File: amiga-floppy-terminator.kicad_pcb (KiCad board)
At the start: 2 copper layers, 7.7 x 59.5 mm, 2 parts, among them J1 Conn_02x17_Odd_Even

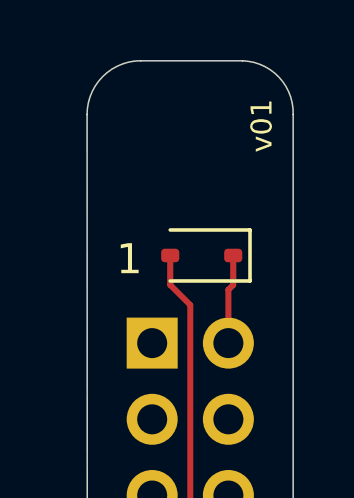
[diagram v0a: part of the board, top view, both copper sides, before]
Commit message: v02: Invert diode polarity
What I could do wrong, I did.

Both _DCD and _SEL0 are active low, hence the diode must be inverted to
point towards _SEL0.
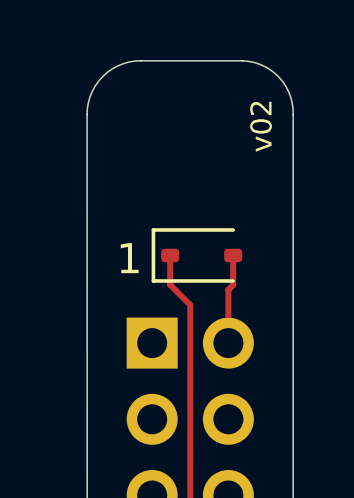
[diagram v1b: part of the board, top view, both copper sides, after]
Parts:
- turned D1 to 0 degrees
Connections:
- D1 pad 1: _DCD -> _SEL0
- D1 pad 2: _SEL0 -> _DCD
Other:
- board text added: "v02"
- board text removed: "v01"
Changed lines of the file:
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@@
 	(footprint "Diode_SMD:D_SOD-323"
 		(layer "F.Cu")
-		(at 101.6 59.563 180)
+		(at 101.6 59.563)
 		(descr "SOD-323")
 		(tags "SOD-323")
 		(property "Reference" "D1"
-			(at 0 -1.85 0)
+			(at 0 -1.85 360)
 			(layer "F.SilkS")
 			(hide yes)
@@
 		)
 		(property "Value" "D"
-			(at 0.1 1.9 0)
+			(at 0.1 1.9 360)
 			(layer "F.Fab")
 			(effects
@@
 		)
 		(property "Footprint" "Diode_SMD:D_SOD-323"
-			(at 0 0 180)
+			(at 0 0 0)
 			(unlocked yes)
 			(layer "F.Fab")
@@
 		)
 		(property "Datasheet" ""
-			(at 0 0 180)
+			(at 0 0 0)
 			(unlocked yes)
 			(layer "F.Fab")
@@
 		)
 		(property "Description" "Diode"
-			(at 0 0 180)
+			(at 0 0 0)
 			(unlocked yes)
 			(layer "F.Fab")
@@
 		)
 		(property "Sim.Device" "D"
-			(at 0 0 180)
+			(at 0 0 0)
 			(unlocked yes)
 			(layer "F.Fab")
@@
 		)
 		(property "Sim.Pins" "1=K 2=A"
-			(at 0 0 180)
+			(at 0 0 0)
 			(unlocked yes)
 			(layer "F.Fab")
@@
 		)
 		(property "LCSC" "C2128"
-			(at 0 0 180)
+			(at 0 0 0)
 			(unlocked yes)
 			(layer "F.Fab")
@@
 		(attr smd)
 		(fp_line
+			(start -1.61 -0.85)
+			(end -1.61 0.85)
+			(stroke
+				(width 0.12)
+				(type solid)
+			)
+			(layer "F.SilkS")
+		)
+		(fp_line
+			(start -1.61 -0.85)
+			(end 1.05 -0.85)
+			(stroke
+				(width 0.12)
+				(type solid)
+			)
+			(layer "F.SilkS")
+		)
+		(fp_line
 			(start -1.61 0.85)
 			(end 1.05 0.85)
@@
 		)
 		(fp_line
-			(start -1.61 -0.85)
-			(end 1.05 -0.85)
-			(stroke
-				(width 0.12)
-				(type solid)
-			)
-			(layer "F.SilkS")
-		)
-		(fp_line
-			(start -1.61 -0.85)
-			(end -1.61 0.85)
-			(stroke
-				(width 0.12)
-				(type solid)
-			)
-			(layer "F.SilkS")
+			(start -1.6 -0.95)
+			(end -1.6 0.95)
+			(stroke
+				(width 0.05)
+				(type solid)
+			)
+			(layer "F.CrtYd")
+		)
+		(fp_line
+			(start -1.6 -0.95)
+			(end 1.6 -0.95)
+			(stroke
+				(width 0.05)
+				(type solid)
+			)
+			(layer "F.CrtYd")
+		)
+		(fp_line
+			(start -1.6 0.95)
+			(end 1.6 0.95)
+			(stroke
+				(width 0.05)
+				(type solid)
+			)
+			(layer "F.CrtYd")
 		)
 		(fp_line
@@
 		)
 		(fp_line
-			(start -1.6 0.95)
-			(end 1.6 0.95)
-			(stroke
-				(width 0.05)
-				(type solid)
-			)
-			(layer "F.CrtYd")
-		)
-		(fp_line
-			(start -1.6 -0.95)
-			(end 1.6 -0.95)
-			(stroke
-				(width 0.05)
-				(type solid)
-			)
-			(layer "F.CrtYd")
-		)
-		(fp_line
-			(start -1.6 -0.95)
-			(end -1.6 0.95)
-			(stroke
-				(width 0.05)
-				(type solid)
-			)
-			(layer "F.CrtYd")
+			(start -0.9 -0.7)
+			(end 0.9 -0.7)
+			(stroke
+				(width 0.1)
+				(type solid)
+			)
+			(layer "F.Fab")
+		)
+		(fp_line
+			(start -0.9 0.7)
+			(end -0.9 -0.7)
+			(stroke
+				(width 0.1)
+				(type solid)
+			)
+			(layer "F.Fab")
+		)
+		(fp_line
+			(start -0.3 -0.35)
+			(end -0.3 0.35)
+			(stroke
+				(width 0.1)
+				(type solid)
+			)
+			(layer "F.Fab")
+		)
+		(fp_line
+			(start -0.3 0)
+			(end -0.5 0)
+			(stroke
+				(width 0.1)
+				(type solid)
+			)
+			(layer "F.Fab")
+		)
+		(fp_line
+			(start -0.3 0)
+			(end 0.2 -0.35)
+			(stroke
+				(width 0.1)
+				(type solid)
+			)
+			(layer "F.Fab")
+		)
+		(fp_line
+			(start 0.2 -0.35)
+			(end 0.2 0.35)
+			(stroke
+				(width 0.1)
+				(type solid)
+			)
+			(layer "F.Fab")
+		)
+		(fp_line
+			(start 0.2 0)
+			(end 0.45 0)
+			(stroke
+				(width 0.1)
+				(type solid)
+			)
+			(layer "F.Fab")
+		)
+		(fp_line
+			(start 0.2 0.35)
+			(end -0.3 0)
+			(stroke
+				(width 0.1)
+				(type solid)
+			)
+			(layer "F.Fab")
+		)
+		(fp_line
+			(start 0.9 -0.7)
+			(end 0.9 0.7)
+			(stroke
+				(width 0.1)
+				(type solid)
+			)
+			(layer "F.Fab")
 		)
 		(fp_line
@@
 			(layer "F.Fab")
 		)
-		(fp_line
-			(start 0.9 -0.7)
-			(end 0.9 0.7)
-			(stroke
-				(width 0.1)
-				(type solid)
-			)
-			(layer "F.Fab")
-		)
-		(fp_line
-			(start 0.2 0.35)
-			(end -0.3 0)
-			(stroke
-				(width 0.1)
-				(type solid)
-			)
-			(layer "F.Fab")
-		)
-		(fp_line
-			(start 0.2 0)
-			(end 0.45 0)
-			(stroke
-				(width 0.1)
-				(type solid)
-			)
-			(layer "F.Fab")
-		)
-		(fp_line
-			(start 0.2 -0.35)
-			(end 0.2 0.35)
-			(stroke
-				(width 0.1)
-				(type solid)
-			)
-			(layer "F.Fab")
-		)
-		(fp_line
-			(start -0.3 0)
-			(end 0.2 -0.35)
-			(stroke
-				(width 0.1)
-				(type solid)
-			)
-			(layer "F.Fab")
-		)
-		(fp_line
-			(start -0.3 0)
-			(end -0.5 0)
-			(stroke
-				(width 0.1)
-				(type solid)
-			)
-			(layer "F.Fab")
-		)
-		(fp_line
-			(start -0.3 -0.35)
-			(end -0.3 0.35)
-			(stroke
-				(width 0.1)
-				(type solid)
-			)
-			(layer "F.Fab")
-		)
-		(fp_line
-			(start -0.9 0.7)
-			(end -0.9 -0.7)
-			(stroke
-				(width 0.1)
-				(type solid)
-			)
-			(layer "F.Fab")
-		)
-		(fp_line
-			(start -0.9 -0.7)
-			(end 0.9 -0.7)
-			(stroke
-				(width 0.1)
-				(type solid)
-			)
-			(layer "F.Fab")
-		)
 		(fp_text user "${REFERENCE}"
-			(at 0 -1.85 0)
+			(at 0 -1.85 360)
 			(layer "F.Fab")
 			(effects
@@
 		)
 		(pad "1" smd roundrect
-			(at -1.05 0 180)
+			(at -1.05 0)
+			(size 0.6 0.45)
+			(layers "F.Cu" "F.Paste" "F.Mask")
+			(roundrect_rratio 0.25)
+			(net 2 "_SEL0")
+			(pinfunction "K")
+			(pintype "passive")
+		)
+		(pad "2" smd roundrect
+			(at 1.05 0)
 			(size 0.6 0.45)
 			(layers "F.Cu" "F.Paste" "F.Mask")
 			(roundrect_rratio 0.25)
 			(net 1 "_DCD")
-			(pinfunction "K")
-			(pintype "passive")
-		)
-		(pad "2" smd roundrect
-			(at 1.05 0 180)
-			(size 0.6 0.45)
-			(layers "F.Cu" "F.Paste" "F.Mask")
-			(roundrect_rratio 0.25)
-			(net 2 "_SEL0")
 			(pinfunction "A")
 			(pintype "passive")
@@
 		)
 	)
-	(gr_text "v01\n"
+	(gr_text "v02\n"
 		(at 104.013 56.134 90)
 		(layer "F.SilkS")
